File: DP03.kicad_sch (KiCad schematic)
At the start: 21 parts

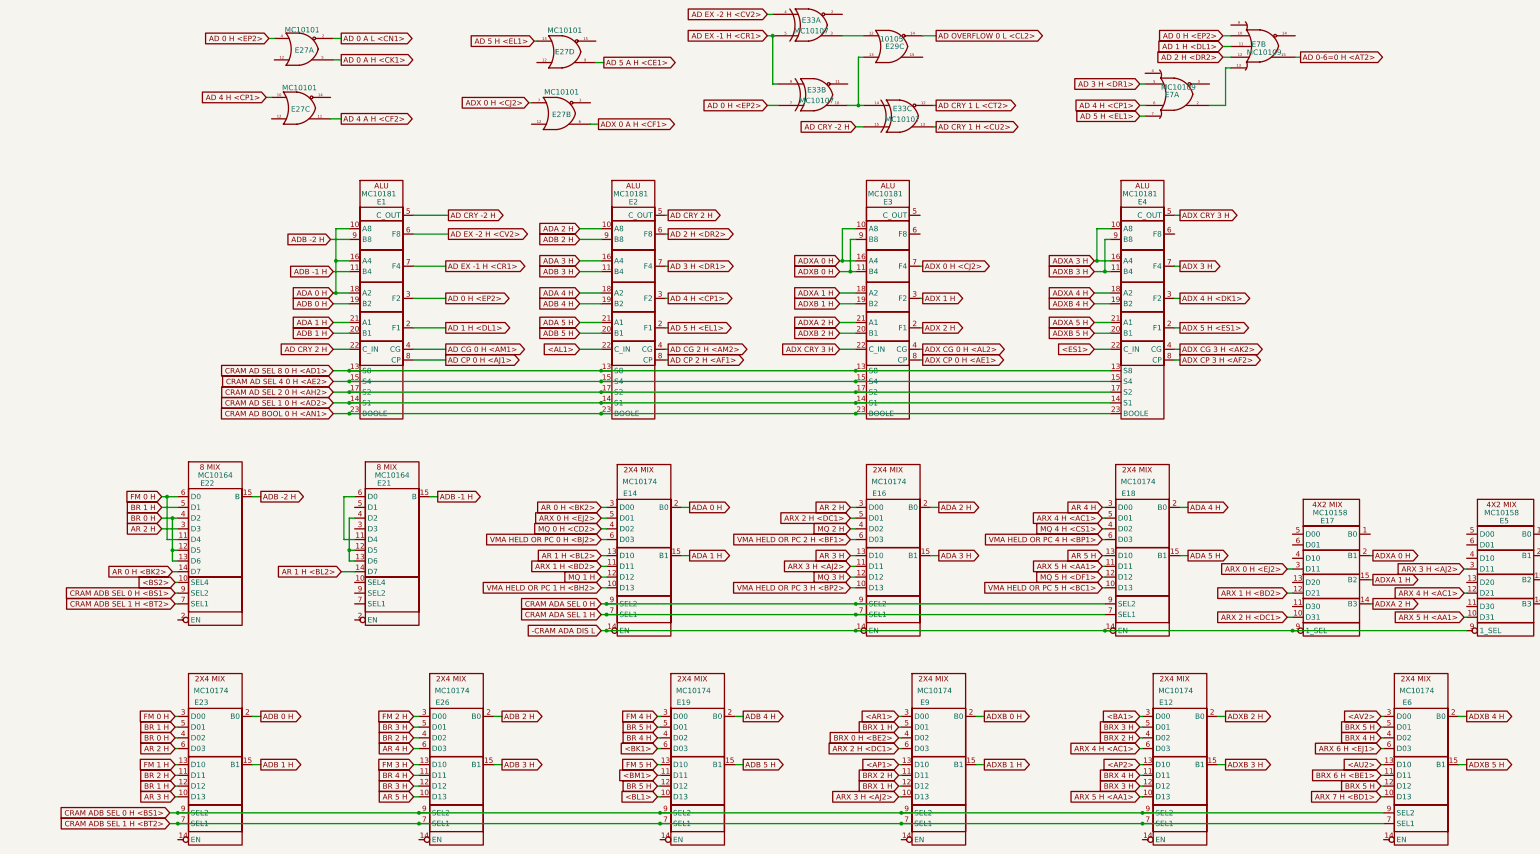
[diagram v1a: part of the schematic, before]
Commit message: Fix a bunch of typos, add ${N} macros for slot specific net names
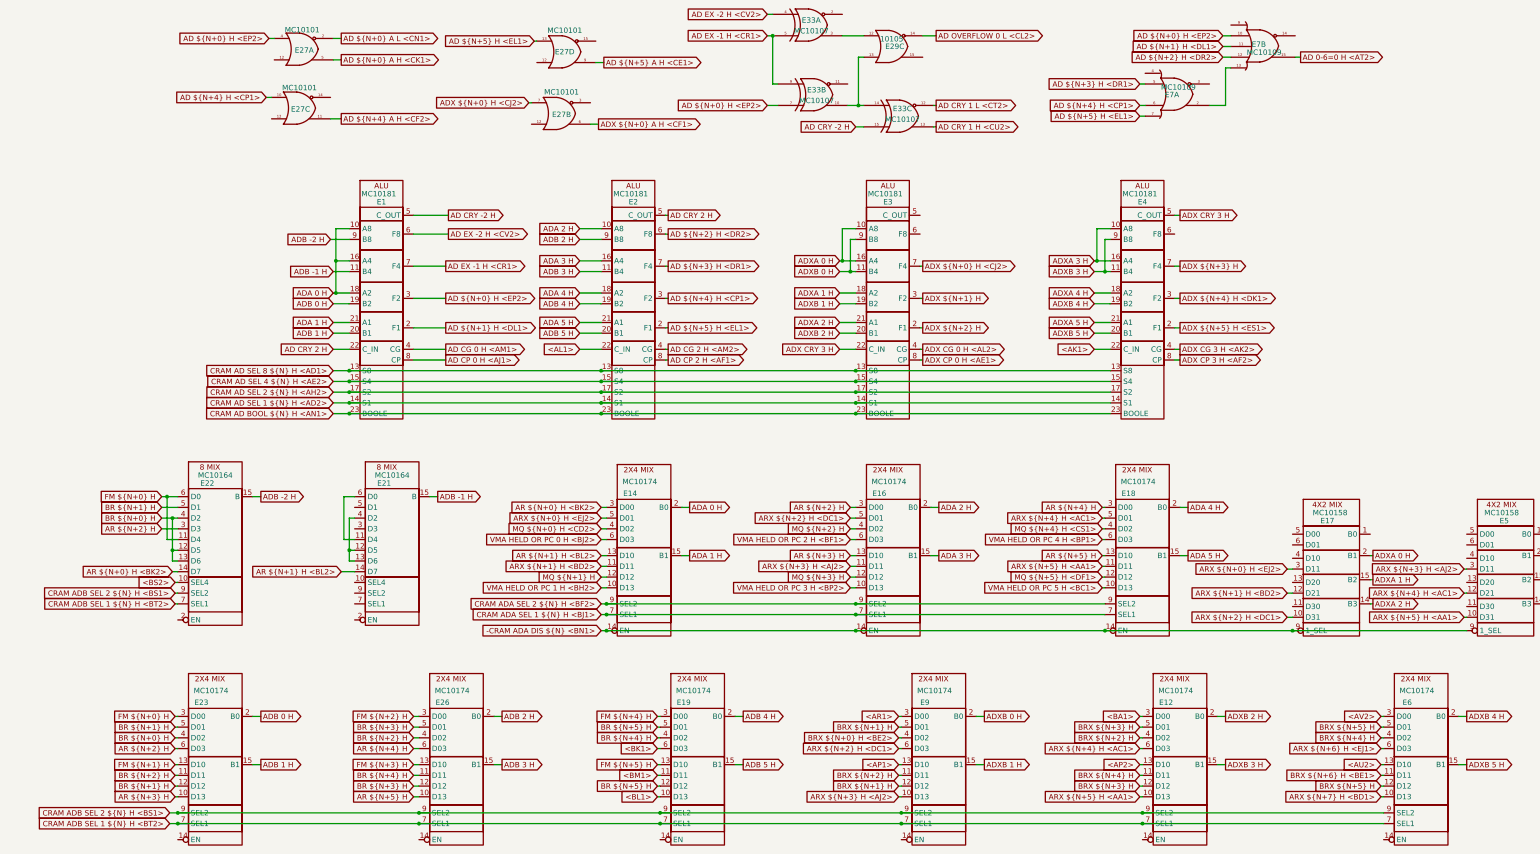
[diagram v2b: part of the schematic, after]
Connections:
- net -CRAM ADA DIS L renamed -CRAM ADA DIS ${N} <BN1>
- net <ES1> renamed <AK1>
- net AD 0 A H <CK1> renamed AD ${N+0} A H <CK1>
- net AD 0 A L <CN1> renamed AD ${N+0} A L <CN1>
- net AD 0 H <EP2> renamed AD ${N+0} H <EP2>
- net AD 1 H <DL1> renamed AD ${N+1} H <DL1>
- net AD 2 H <DR2> renamed AD ${N+2} H <DR2>
- net AD 3 H <DR1> renamed AD ${N+3} H <DR1>
- net AD 4 A H <CF2> renamed AD ${N+4} A H <CF2>
- net AD 4 H <CP1> renamed AD ${N+4} H <CP1>
- net AD 5 A H <CE1> renamed AD ${N+5} A H <CE1>
- net AD 5 H <EL1> renamed AD ${N+5} H <EL1>
- net ADX 0 A H <CF1> renamed ADX ${N+0} A H <CF1>
- net ADX 0 H <CJ2> renamed ADX ${N+0} H <CJ2>
- net ADX 1 H renamed ADX ${N+1} H
- net ADX 2 H renamed ADX ${N+2} H
- net ADX 3 H renamed ADX ${N+3} H
- net ADX 4 H <DK1> renamed ADX ${N+4} H <DK1>
- net ADX 5 H <ES1> renamed ADX ${N+5} H <ES1>
- net AR 0 H <BK2> renamed AR ${N+0} H <BK2>
- net AR 1 H <BL2> renamed AR ${N+1} H <BL2>
- net AR 2 H renamed AR ${N+2} H
- net AR 3 H renamed AR ${N+3} H
- net AR 4 H renamed AR ${N+4} H
- net AR 5 H renamed AR ${N+5} H
- net ARX 0 H <EJ2> renamed ARX ${N+0} H <EJ2>
- net ARX 1 H <BD2> renamed ARX ${N+1} H <BD2>
- net ARX 2 H <DC1> renamed ARX ${N+2} H <DC1>
- net ARX 3 H <AJ2> renamed ARX ${N+3} H <AJ2>
- net ARX 4 H <AC1> renamed ARX ${N+4} H <AC1>
- net ARX 5 H <AA1> renamed ARX ${N+5} H <AA1>
- net ARX 6 H <EJ1> renamed ARX ${N+6} H <EJ1>
- net ARX 7 H <BD1> renamed ARX ${N+7} H <BD1>
- net BR 0 H renamed BR ${N+0} H
- net BR 1 H renamed BR ${N+1} H
- net BR 2 H renamed BR ${N+2} H
- net BR 3 H renamed BR ${N+3} H
- net BR 4 H renamed BR ${N+4} H
- net BR 5 H renamed BR ${N+5} H
- net BRX 0 H <BE2> renamed BRX ${N+0} H <BE2>
- net BRX 1 H renamed BRX ${N+1} H
- net BRX 2 H renamed BRX ${N+2} H
- net BRX 3 H renamed BRX ${N+3} H
- net BRX 4 H renamed BRX ${N+4} H
- net BRX 5 H renamed BRX ${N+5} H
- net BRX 6 H <BE1> renamed BRX ${N+6} H <BE1>
- net CRAM AD BOOL 0 H <AN1> renamed CRAM AD BOOL ${N} H <AN1>
- net CRAM AD SEL 1 0 H <AD2> renamed CRAM AD SEL 1 ${N} H <AD2>
- net CRAM AD SEL 2 0 H <AH2> renamed CRAM AD SEL 2 ${N} H <AH2>
- net CRAM AD SEL 4 0 H <AE2> renamed CRAM AD SEL 4 ${N} H <AE2>
- net CRAM AD SEL 8 0 H <AD1> renamed CRAM AD SEL 8 ${N} H <AD1>
- net CRAM ADA SEL 0 H renamed CRAM ADA SEL 2 ${N} H <BF2>
- net CRAM ADA SEL 1 H renamed CRAM ADA SEL 1 ${N} H <BJ1>
- net CRAM ADB SEL 0 H <BS1> renamed CRAM ADB SEL 2 ${N} H <BS1>
- net CRAM ADB SEL 1 H <BT2> renamed CRAM ADB SEL 1 ${N} H <BT2>
- net FM 0 H renamed FM ${N+0} H
- net FM 1 H renamed FM ${N+1} H
- net FM 2 H renamed FM ${N+2} H
- net FM 3 H renamed FM ${N+3} H
- net FM 4 H renamed FM ${N+4} H
- net FM 5 H renamed FM ${N+5} H
- net MQ 0 H <CD2> renamed MQ ${N+0} H <CD2>
- net MQ 1 H renamed MQ ${N+1} H
- net MQ 2 H renamed MQ ${N+2} H
- net MQ 3 H renamed MQ ${N+3} H
- net MQ 4 H <CS1> renamed MQ ${N+4} H <CS1>
- net MQ 5 H <DF1> renamed MQ ${N+5} H <DF1>

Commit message: I think all pages now have ${N+x} stuff, but still need to relabel J1 net names to match.
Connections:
- net <AK1> renamed ${N/30+1, ADX CRY ${N+6} H, CTL ADX CRY 36 H} <AK1>
- net <AL1> renamed ${N/30+1, AD CRY ${N+6} H, AD CRY 36 B H} <AL1>
- net <AP1> renamed # ${N+1} H <AP1>
- net <AP2> renamed # ${N+3} H <AP2>
- net <AR1> renamed # ${N+0} <AR1>
- net <AU2> renamed # ${N+5} H <AU2>
- net <AV2> renamed # ${N+4} H <AV2>
- net <BA1> renamed # ${N+2} H <BA1>
- net <BK1> renamed ${N/30+1, AR ${N+6} H, ARX 00 H} <BK1>
- net <BL1> renamed ${N/30+1, AR ${N+7} h, ARX 01 H} <BL1>
- net <BM1> renamed ${N/30+1 BR ${N+6} A H, BRX 00 H} <BM1>
- net <BS2> renamed ${(N+199)/100, HI, NC} <BS2>
- net AD 0-6=0 H <AT2> renamed AD ${N+0}-${N+5}=0 H <AT2>
- net AD CG 0 H <AM1> renamed AD CG ${N+0} H <AM1>
- net AD CG 2 H <AM2> renamed AD CG ${N+2} H <AM2>
- net AD CP 0 H <AJ1> renamed AD CP ${N+0} H <AJ1>
- net AD CP 2 H <AF1> renamed AD CP ${N+2} H <AF1>
- net AD CRY -2 H renamed AD CRY ${N-2} H
- net AD CRY 1 H <CU2> renamed AD CRY ${N+1} H <CU2>
- net AD CRY 1 L <CT2> renamed AD CRY ${N+1} L <CT2>
- net AD CRY 2 H renamed AD CRY ${N+2} H
- net AD EX -1 H <CR1> renamed AD EX ${N-1} H <CR1>
- net AD EX -2 H <CV2> renamed AD EX ${N-2} H <CV2>
- net AD OVERFLOW 0 L <CL2> renamed AD OVERFLOW ${N} L <CL2>
- net ADA 0 H renamed ADA ${N+0} H
- net ADA 1 H renamed ADA ${N+1} H
- net ADA 2 H renamed ADA ${N+2} H
- net ADA 3 H renamed ADA ${N+3} H
- net ADA 4 H renamed ADA ${N+4} H
- net ADA 5 H renamed ADA ${N+5} H
- net ADB -1 H renamed ADB ${N-1} H
- net ADB -2 H renamed ADB ${N-2} H
- net ADB 0 H renamed ADB ${N+0} H
- net ADB 1 H renamed ADB ${N+1} H
- net ADB 2 H renamed ADB ${N+2} H
- net ADB 3 H renamed ADB ${N+3} H
- net ADB 4 H renamed ADB ${N+4} H
- net ADB 5 H renamed ADB ${N+5} H
- net ADX CG 0 H <AL2> renamed ADX CG ${N+0} H <AL2>
- net ADX CG 3 H <AK2> renamed ADX CG ${N+3} H <AK2>
- net ADX CP 0 H <AE1> renamed ADX CP ${N+0} H <AE1>
- net ADX CP 3 H <AF2> renamed ADX CP ${N+3} H <AF2>
- net ADX CRY 3 H renamed ADX CRY ${N+3} H
- net ADXA 0 H renamed ADXA ${N+0} H
- net ADXA 1 H renamed ADXA ${N+1} H
- net ADXA 2 H renamed ADXA ${N+2} H
- net ADXA 3 H renamed ADXA ${N+3} H
- net ADXA 4 H renamed ADXA ${N+4} H
- net ADXA 5 H renamed ADXA ${N+5} H
- net ADXB 0 H renamed ADXB ${N+0} H
- net ADXB 1 H renamed ADXB ${N+1} H
- net ADXB 2 H renamed ADXB ${N+2} H
- net ADXB 3 H renamed ADXB ${N+3} H
- net ADXB 4 H renamed ADXB ${N+4} H
- net ADXB 5 H renamed ADXB ${N+5} H
- net VMA HELD OR PC 3 H <BP2> renamed VMA HELD OR PC ${N+3} H <BP2>
- net VMA HELD OR PC 5 H <BC1> renamed VMA HELD OR PC ${N+5} H <BC1>
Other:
- moved on the sheet: E1, E12, E14, E16, E17, E18, E2, E21, E22, E3, E5, E6

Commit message: Remove "slash" in several places as an experiment. it did not work.
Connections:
- net ${(N+199)/100, HI, NC} <BS2> renamed ${(N+199)/100, HI, NC} <BS2>
- net ${N/30+1 BR ${N+6} A H, BRX 00 H} <BM1> renamed ${N/30+1 BR ${N+6} A H, BRX 00 H} <BM1>
- net ${N/30+1, AD CRY ${N+6} H, AD CRY 36 B H} <AL1> renamed ${N/30+1, AD CRY ${N+6} H, AD CRY 36 B H} <AL1>
- net ${N/30+1, ADX CRY ${N+6} H, CTL ADX CRY 36 H} <AK1> renamed ${N/30+1, ADX CRY ${N+6} H, CTL ADX CRY 36 H} <AK1>
- net ${N/30+1, AR ${N+6} H, ARX 00 H} <BK1> renamed ${N/30+1, AR ${N+6} H, ARX 00 H} <BK1>
- net ${N/30+1, AR ${N+7} h, ARX 01 H} <BL1> renamed ${N/30+1, AR ${N+7} h, ARX 01 H} <BL1>
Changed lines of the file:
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@@
     )
   )
-  (global_label "${N{slash}30+1, AR ${N+7} h, ARX 01 H} <BL1>" (shape input) (at 184.785 234.95 180) (fields_autoplaced)
+  (global_label "${N/30+1, AR ${N+7} h, ARX 01 H} <BL1>" (shape input) (at 184.785 234.95 180) (fields_autoplaced)
     (effects (font (size 1.27 1.27)) (justify right))
     (property "Intersheet References" "${INTERSHEET_REFS}" (id 0) (at 133.749 234.8706 0)
@@
     )
   )
-  (global_label "${N{slash}30+1 BR ${N+6} A H, BRX 00 H} <BM1>" (shape input) (at 184.785 231.14 180) (fields_autoplaced)
+  (global_label "${N/30+1 BR ${N+6} A H, BRX 00 H} <BM1>" (shape input) (at 184.785 231.14 180) (fields_autoplaced)
     (effects (font (size 1.27 1.27)) (justify right))
     (property "Intersheet References" "${INTERSHEET_REFS}" (id 0) (at 131.33 231.0606 0)
@@
     )
   )
-  (global_label "${N{slash}30+1, AD CRY ${N+6} H, AD CRY 36 B H} <AL1>" (shape input)
-    (at 138.43 128.27 0) (fields_autoplaced)
+  (global_label "${N/30+1, AD CRY ${N+6} H, AD CRY 36 B H} <AL1>" (shape input) (at 138.43 128.27 180) (fields_autoplaced)
     (effects (font (size 1.27 1.27)) (justify right))
     (property "Intersheet References" "${INTERSHEET_REFS}" (id 0) (at 77.1736 128.1906 0)
@@
     )
   )
-  (global_label "${(N+199){slash}100, HI, NC} <BS2>" (shape input) (at 50.8 162.56 180) (fields_autoplaced)
+  (global_label "${(N+199)/100, HI, NC} <BS2>" (shape input) (at 50.8 162.56 180) (fields_autoplaced)
     (effects (font (size 1.27 1.27)) (justify right))
     (property "Intersheet References" "${INTERSHEET_REFS}" (id 0) (at 11.4359 162.4806 0)
@@
     )
   )
-  (global_label "${N{slash}30+1, AR ${N+6} H, ARX 00 H} <BK1>" (shape input) (at 191.135 180.975 180) (fields_autoplaced)
+  (global_label "${N/30+1, AR ${N+6} H, ARX 00 H} <BK1>" (shape input) (at 191.135 180.975 180) (fields_autoplaced)
     (effects (font (size 1.27 1.27)) (justify right))
     (property "Intersheet References" "${INTERSHEET_REFS}" (id 0) (at 139.6757 180.8956 0)
@@
     )
   )
-  (global_label "${N{slash}30+1, ADX CRY ${N+6} H, CTL ADX CRY 36 H} <AK1>" (shape input)
+  (global_label "${N/30+1, ADX CRY ${N+6} H, CTL ADX CRY 36 H} <AK1>" (shape input)
     (at 296.545 128.905 0) (fields_autoplaced)
     (effects (font (size 1.27 1.27)) (justify right))

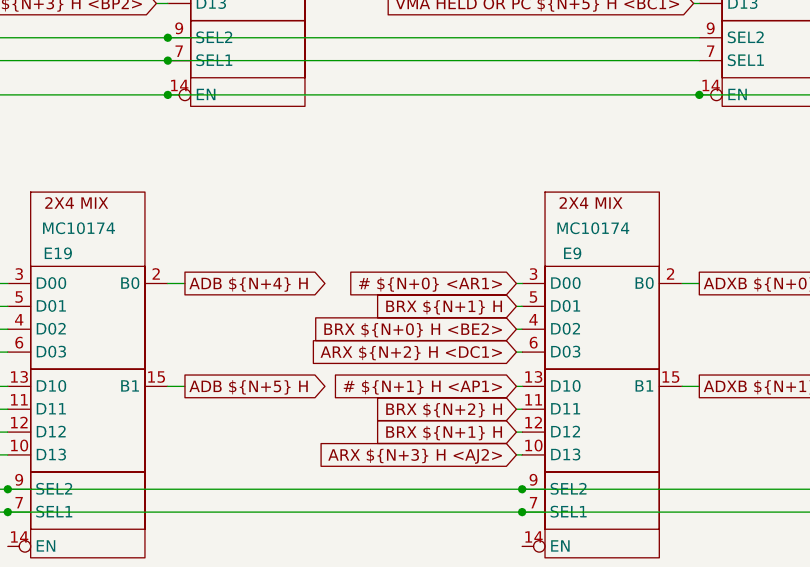
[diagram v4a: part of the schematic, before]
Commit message: Fix <AR1> net name, fix up borked label
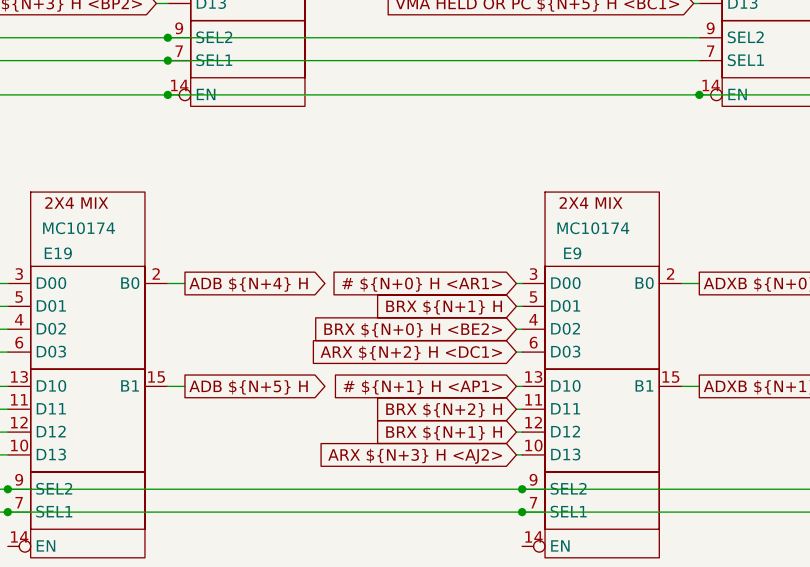
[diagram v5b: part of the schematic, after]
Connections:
- net # ${N+0} <AR1> renamed # ${N+0} H <AR1>
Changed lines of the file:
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@@
     )
   )
-  (global_label "# ${N+0} <AR1>" (shape input) (at 250.825 194.945 180) (fields_autoplaced)
+  (global_label "# ${N+0} H <AR1>" (shape input) (at 250.825 194.945 180) (fields_autoplaced)
     (effects (font (size 1.27 1.27)) (justify right))
-    (property "Intersheet References" "${INTERSHEET_REFS}" (id 0) (at 231.4786 194.8656 0)
+    (property "Intersheet References" "${INTERSHEET_REFS}" (id 0) (at 229.1805 194.8656 0)
       (effects (font (size 1.27 1.27)) (justify right) hide)
     )
